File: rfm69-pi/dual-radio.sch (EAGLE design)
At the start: 7 parts, among them U1 RFM69HCW, U2 RFM69HCW, X1 BU-SMA-G, X2 RASPI_BOARD_B+#_HDC, X3 BU-SMA-G, X4 SMA-142-0701-871/876, X5 SMA-142-0701-871/876

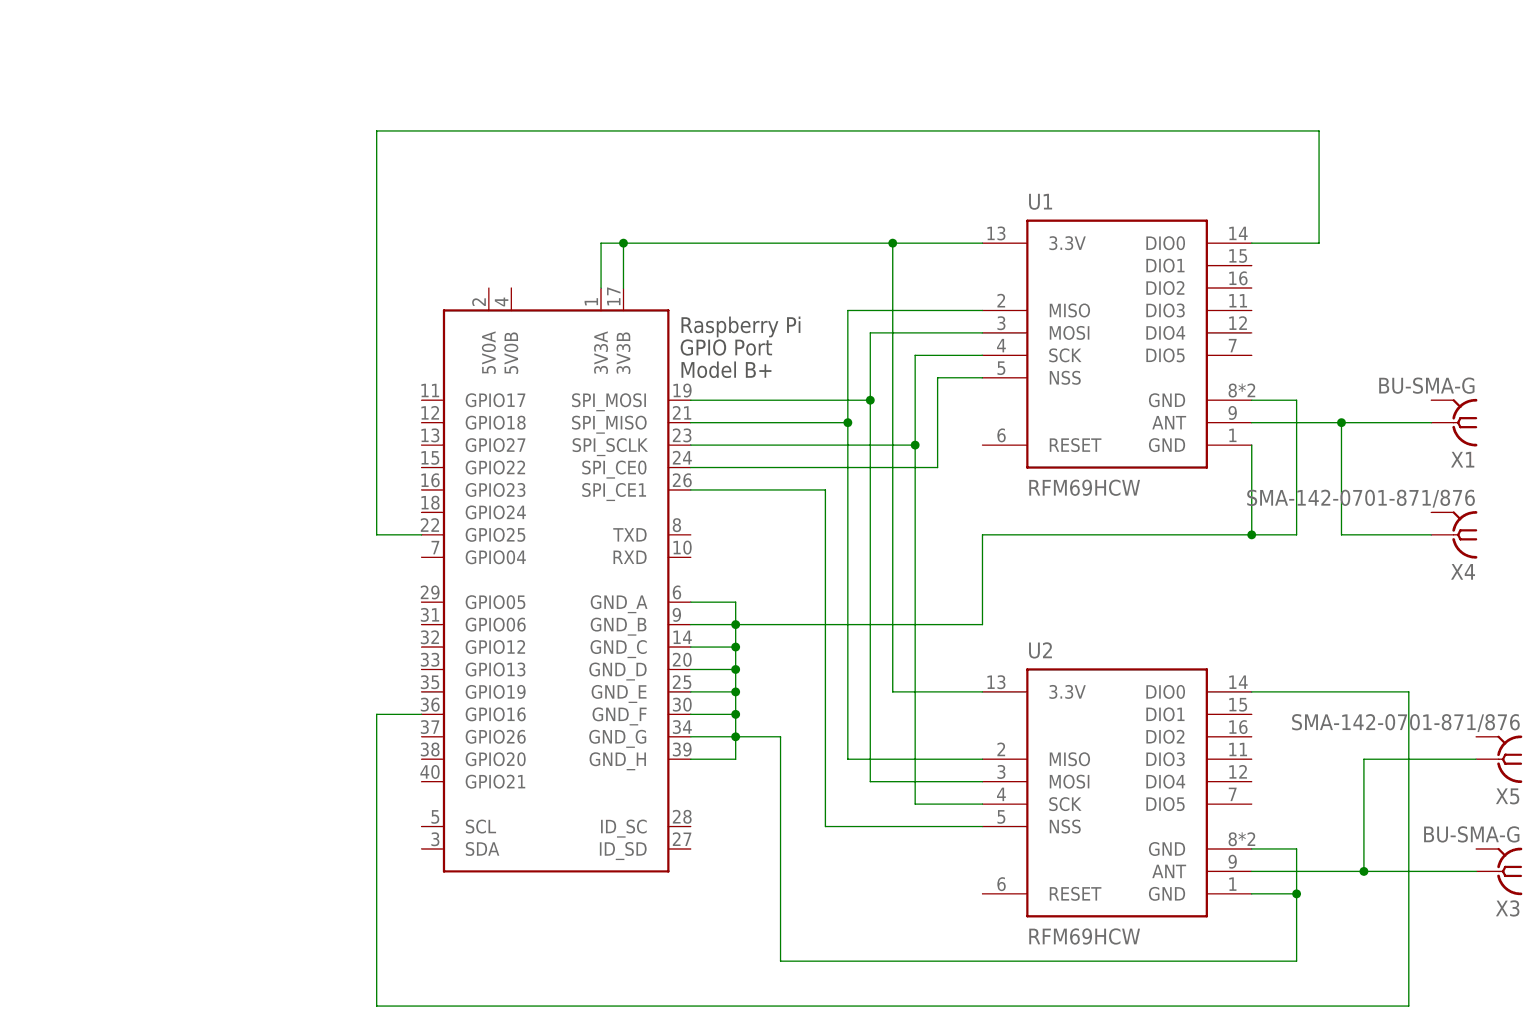
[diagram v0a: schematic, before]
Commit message: Fix boards and add the pi control station
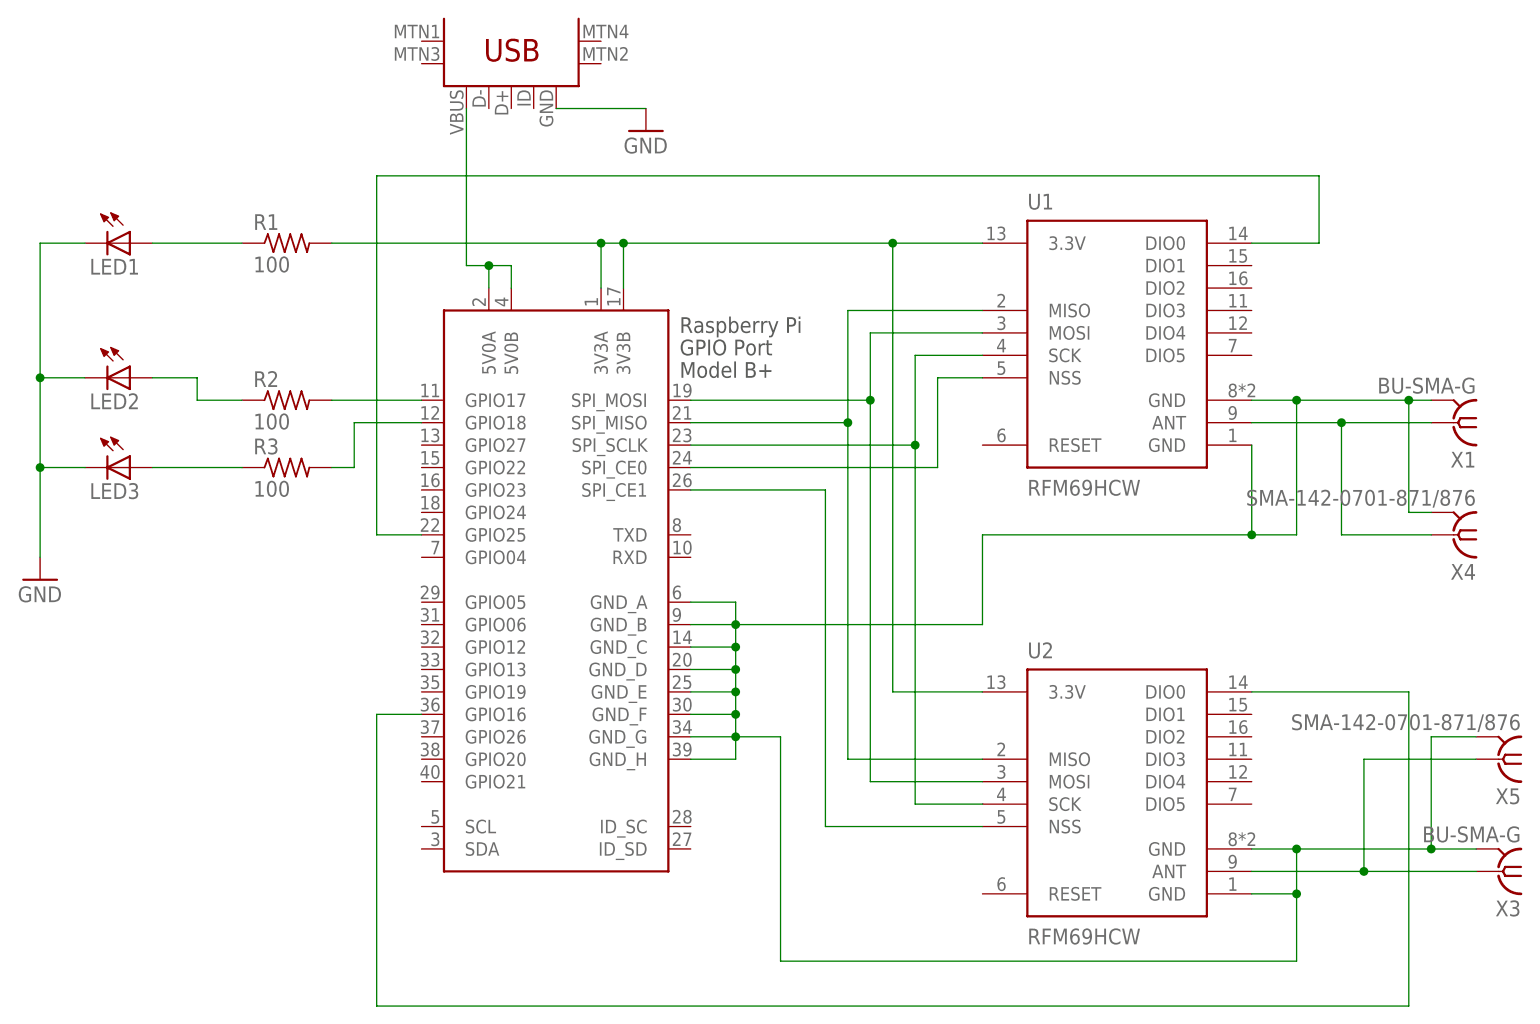
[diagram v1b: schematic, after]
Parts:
- added LED1, LED2, LED3: (no value), led:LEDSML0805
- added R1, R2, R3: 100, resistor:R-US_M0805
- added U$1: USB-MINIB-5PIN, SparkFun-Connectors:USB-MINIB-5PIN
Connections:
- new net GND: LED1.C, LED2.C, LED3.C, U$1.GND
- new net N$12: R2.2, X2.GPIO17
- new net N$13: R3.2, X2.GPIO18
- new net N$14: LED1.A, R1.1
- new net N$15: LED2.A, R2.1
- new net N$16: LED3.A, R3.1
- new net N$17: U$1.VBUS, X2.5V0A, X2.5V0B
- net N$1: now also R1.2
- net N$7: now also X1.2, X3.2, X4.2, X5.2
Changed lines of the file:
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@@
 <part name="X4" library="con-coax" deviceset="SMA-" device="142-0701-871/876"/>
 <part name="X5" library="con-coax" deviceset="SMA-" device="142-0701-871/876"/>
+<part name="R1" library="resistor" deviceset="R-US_" device="M0805" value="100"/>
+<part name="R2" library="resistor" deviceset="R-US_" device="M0805" value="100"/>
+<part name="R3" library="resistor" deviceset="R-US_" device="M0805" value="100"/>
+<part name="LED1" library="led" deviceset="LED" device="SML0805"/>
+<part name="LED2" library="led" deviceset="LED" device="SML0805"/>
+<part name="LED3" library="led" deviceset="LED" device="SML0805"/>
+<part name="GND1" library="SparkFun-Aesthetics" deviceset="GND" device=""/>
+<part name="U$1" library="SparkFun-Connectors" deviceset="USB-MINIB" device="-5PIN"/>
+<part name="GND2" library="SparkFun-Aesthetics" deviceset="GND" device=""/>
 </parts>
 <sheets>
@@
 <instance part="X4" gate="G1" x="132.08" y="53.34" rot="R180"/>
 <instance part="X5" gate="G1" x="137.16" y="27.94" rot="R180"/>
+<instance part="R1" gate="G$1" x="0" y="86.36"/>
+<instance part="R2" gate="G$1" x="0" y="68.58"/>
+<instance part="R3" gate="G$1" x="0" y="60.96"/>
+<instance part="LED1" gate="G$1" x="-17.78" y="86.36" rot="R270"/>
+<instance part="LED2" gate="G$1" x="-17.78" y="71.12" rot="R270"/>
+<instance part="LED3" gate="G$1" x="-17.78" y="60.96" rot="R270"/>
+<instance part="GND1" gate="1" x="-27.94" y="48.26"/>
+<instance part="U$1" gate="G$1" x="30.48" y="104.14" rot="R90"/>
+<instance part="GND2" gate="1" x="40.64" y="99.06"/>
 </instances>
 <busses>
@@
 <wire x1="35.56" y1="86.36" x2="38.1" y2="86.36" width="0.1524" layer="91"/>
 <junction x="38.1" y="86.36"/>
+<pinref part="R1" gate="G$1" pin="2"/>
+<wire x1="5.08" y1="86.36" x2="35.56" y2="86.36" width="0.1524" layer="91"/>
+<junction x="35.56" y="86.36"/>
 </segment>
 </net>
@@
 <pinref part="X2" gate="G$1" pin="GND_G"/>
 <pinref part="X2" gate="G$1" pin="GND_H"/>
+<pinref part="X1" gate="G1" pin="2"/>
+<wire x1="114.3" y1="68.58" x2="127" y2="68.58" width="0.1524" layer="91"/>
+<junction x="114.3" y="68.58"/>
+<wire x1="127" y1="68.58" x2="129.54" y2="68.58" width="0.1524" layer="91"/>
+<wire x1="127" y1="68.58" x2="127" y2="55.88" width="0.1524" layer="91"/>
+<junction x="127" y="68.58"/>
+<pinref part="X4" gate="G1" pin="2"/>
+<wire x1="127" y1="55.88" x2="129.54" y2="55.88" width="0.1524" layer="91"/>
+<pinref part="X3" gate="G1" pin="2"/>
+<wire x1="114.3" y1="17.78" x2="129.54" y2="17.78" width="0.1524" layer="91"/>
+<junction x="114.3" y="17.78"/>
+<wire x1="129.54" y1="17.78" x2="134.62" y2="17.78" width="0.1524" layer="91"/>
+<wire x1="129.54" y1="17.78" x2="129.54" y2="30.48" width="0.1524" layer="91"/>
+<junction x="129.54" y="17.78"/>
+<pinref part="X5" gate="G1" pin="2"/>
+<wire x1="129.54" y1="30.48" x2="134.62" y2="30.48" width="0.1524" layer="91"/>
 </segment>
 </net>
 <net name="N$8" class="0">
 <segment>
-<wire x1="10.16" y1="53.34" x2="10.16" y2="99.06" width="0.1524" layer="91"/>
-<wire x1="10.16" y1="99.06" x2="116.84" y2="99.06" width="0.1524" layer="91"/>
-<wire x1="116.84" y1="99.06" x2="116.84" y2="86.36" width="0.1524" layer="91"/>
+<wire x1="10.16" y1="53.34" x2="10.16" y2="93.98" width="0.1524" layer="91"/>
+<wire x1="10.16" y1="93.98" x2="116.84" y2="93.98" width="0.1524" layer="91"/>
+<wire x1="116.84" y1="93.98" x2="116.84" y2="86.36" width="0.1524" layer="91"/>
 <pinref part="U1" gate="G$1" pin="DIO0"/>
 <wire x1="116.84" y1="86.36" x2="109.22" y2="86.36" width="0.1524" layer="91"/>
@@
 </segment>
 </net>
+<net name="N$12" class="0">
+<segment>
+<pinref part="R2" gate="G$1" pin="2"/>
+<pinref part="X2" gate="G$1" pin="GPIO17"/>
+<wire x1="5.08" y1="68.58" x2="15.24" y2="68.58" width="0.1524" layer="91"/>
+</segment>
+</net>
+<net name="N$13" class="0">
+<segment>
+<pinref part="R3" gate="G$1" pin="2"/>
+<wire x1="5.08" y1="60.96" x2="7.62" y2="60.96" width="0.1524" layer="91"/>
+<wire x1="7.62" y1="60.96" x2="7.62" y2="66.04" width="0.1524" layer="91"/>
+<pinref part="X2" gate="G$1" pin="GPIO18"/>
+<wire x1="7.62" y1="66.04" x2="15.24" y2="66.04" width="0.1524" layer="91"/>
+</segment>
+</net>
+<net name="N$14" class="0">
+<segment>
+<pinref part="LED1" gate="G$1" pin="A"/>
+<pinref part="R1" gate="G$1" pin="1"/>
+<wire x1="-15.24" y1="86.36" x2="-5.08" y2="86.36" width="0.1524" layer="91"/>
+</segment>
+</net>
+<net name="N$15" class="0">
+<segment>
+<pinref part="LED2" gate="G$1" pin="A"/>
+<wire x1="-15.24" y1="71.12" x2="-10.16" y2="71.12" width="0.1524" layer="91"/>
+<wire x1="-10.16" y1="71.12" x2="-10.16" y2="68.58" width="0.1524" layer="91"/>
+<pinref part="R2" gate="G$1" pin="1"/>
+<wire x1="-10.16" y1="68.58" x2="-5.08" y2="68.58" width="0.1524" layer="91"/>
+</segment>
+</net>
+<net name="N$16" class="0">
+<segment>
+<pinref part="LED3" gate="G$1" pin="A"/>
+<pinref part="R3" gate="G$1" pin="1"/>
+<wire x1="-15.24" y1="60.96" x2="-5.08" y2="60.96" width="0.1524" layer="91"/>
+</segment>
+</net>
+<net name="GND" class="0">
+<segment>
+<pinref part="LED1" gate="G$1" pin="C"/>
+<pinref part="GND1" gate="1" pin="GND"/>
+<wire x1="-22.86" y1="86.36" x2="-27.94" y2="86.36" width="0.1524" layer="91"/>
+<wire x1="-27.94" y1="86.36" x2="-27.94" y2="71.12" width="0.1524" layer="91"/>
+<pinref part="LED2" gate="G$1" pin="C"/>
+<wire x1="-27.94" y1="71.12" x2="-27.94" y2="60.96" width="0.1524" layer="91"/>
+<wire x1="-27.94" y1="60.96" x2="-27.94" y2="50.8" width="0.1524" layer="91"/>
+<wire x1="-22.86" y1="71.12" x2="-27.94" y2="71.12" width="0.1524" layer="91"/>
+<junction x="-27.94" y="71.12"/>
+<pinref part="LED3" gate="G$1" pin="C"/>
+<wire x1="-22.86" y1="60.96" x2="-27.94" y2="60.96" width="0.1524" layer="91"/>
+<junction x="-27.94" y="60.96"/>
+</segment>
+<segment>
+<pinref part="U$1" gate="G$1" pin="GND"/>
+<pinref part="GND2" gate="1" pin="GND"/>
+<wire x1="30.48" y1="101.6" x2="40.64" y2="101.6" width="0.1524" layer="91"/>
+</segment>
+</net>
+<net name="N$17" class="0">
+<segment>
+<pinref part="U$1" gate="G$1" pin="VBUS"/>
+<wire x1="20.32" y1="101.6" x2="20.32" y2="83.82" width="0.1524" layer="91"/>
+<pinref part="X2" gate="G$1" pin="5V0A"/>
+<wire x1="20.32" y1="83.82" x2="22.86" y2="83.82" width="0.1524" layer="91"/>
+<wire x1="22.86" y1="83.82" x2="22.86" y2="81.28" width="0.1524" layer="91"/>
+<pinref part="X2" gate="G$1" pin="5V0B"/>
+<wire x1="25.4" y1="81.28" x2="25.4" y2="83.82" width="0.1524" layer="91"/>
+<wire x1="25.4" y1="83.82" x2="22.86" y2="83.82" width="0.1524" layer="91"/>
+<junction x="22.86" y="83.82"/>
+</segment>
+</net>
 </nets>
 </sheet>
 </sheets>
+<errors>
+</errors>
 </schematic>
 </drawing>
